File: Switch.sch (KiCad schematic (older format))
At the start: 4 parts, among them SW801 KH-PS1611-54

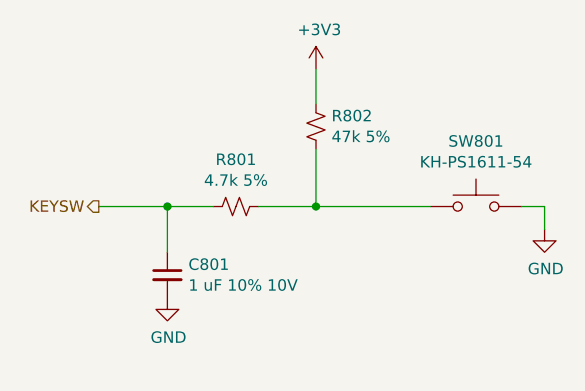
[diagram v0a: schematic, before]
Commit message: Added PCA9745B16B. Updated schematic. ERC Passes.
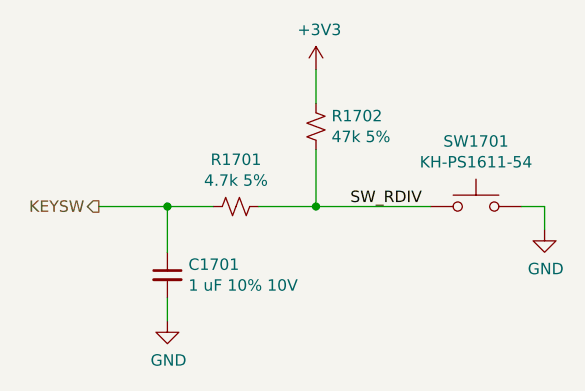
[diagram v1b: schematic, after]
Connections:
- net SW_RDIV: now reaches R801.1, R802.2, SW801.1
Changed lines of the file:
@@
 AR Path="/61A0B595/61A14F2D/61A0C35F" Ref="SW1601"  Part="1"
 AR Path="/61A0B595/61A14FBD/61A0C35F" Ref="SW1701"  Part="1"
-F 0 "SW801" H 5350 3285 50  0000 C CNN
+F 0 "SW1701" H 5350 3285 50  0000 C CNN
 F 1 "KH-PS1611-54" H 5350 3194 50  0000 C CNN
 F 2 "TMPPCB_R2:SW_MX" H 5350 3200 50  0001 C CNN
@@
 AR Path="/61A0B595/61A14F2D/61A0CD9F" Ref="#PWR01603"  Part="1"
 AR Path="/61A0B595/61A14FBD/61A0CD9F" Ref="#PWR01703"  Part="1"
-F 0 "#PWR0803" H 5650 2850 50  0001 C CNN
+F 0 "#PWR01703" H 5650 2850 50  0001 C CNN
 F 1 "GND" H 5655 2927 50  0000 C CNN
 F 2 "" H 5650 3100 50  0001 C CNN
@@
 	1    0    0    -1
 $EndComp
-Wire Wire Line
-	5550 3000 5650 3000
-Wire Wire Line
-	5650 3000 5650 3100
 $Comp
 L power:+3V3 #PWR0802
@@
 AR Path="/61A0B595/61A14F2D/61A0DCFF" Ref="#PWR01602"  Part="1"
 AR Path="/61A0B595/61A14FBD/61A0DCFF" Ref="#PWR01702"  Part="1"
-F 0 "#PWR0802" H 4650 2250 50  0001 C CNN
+F 0 "#PWR01702" H 4650 2250 50  0001 C CNN
 F 1 "+3V3" H 4665 2573 50  0000 C CNN
 F 2 "" H 4650 2400 50  0001 C CNN
@@
 AR Path="/61A0B595/61A14F2D/61A0F3A7" Ref="R1602"  Part="1"
 AR Path="/61A0B595/61A14FBD/61A0F3A7" Ref="R1702"  Part="1"
-F 0 "R802" H 4718 2696 50  0000 L CNN
+F 0 "R1702" H 4718 2696 50  0000 L CNN
 F 1 "47k 5%" H 4718 2605 50  0000 L CNN
 F 2 "Resistor_SMD:R_0805_2012Metric_Pad1.20x1.40mm_HandSolder" H 4650 2650 50  0001 C CNN
@@
 AR Path="/61A0B595/61A14F2D/61A1015C" Ref="C1601"  Part="1"
 AR Path="/61A0B595/61A14FBD/61A1015C" Ref="C1701"  Part="1"
-F 0 "C801" H 4092 3346 50  0000 L CNN
+F 0 "C1701" H 4092 3346 50  0000 L CNN
 F 1 "1 uF 10% 10V" H 4092 3255 50  0000 L CNN
 F 2 "Capacitor_SMD:C_0805_2012Metric_Pad1.18x1.45mm_HandSolder" H 4000 3300 50  0001 C CNN
@@
 L power:GND #PWR0801
 U 1 1 61A104A3
-P 4000 3400
+P 4000 3500
 AR Path="/61A0B595/61A0B6A8/61A104A3" Ref="#PWR0801"  Part="1"
 AR Path="/61A0B595/61A148A8/61A104A3" Ref="#PWR?"  Part="1"
@@
 AR Path="/61A0B595/61A14F2D/61A104A3" Ref="#PWR01601"  Part="1"
 AR Path="/61A0B595/61A14FBD/61A104A3" Ref="#PWR01701"  Part="1"
-F 0 "#PWR0801" H 4000 3150 50  0001 C CNN
-F 1 "GND" H 4005 3227 50  0000 C CNN
-F 2 "" H 4000 3400 50  0001 C CNN
-F 3 "" H 4000 3400 50  0001 C CNN
-	1    4000 3400
+F 0 "#PWR01701" H 4000 3250 50  0001 C CNN
+F 1 "GND" H 4005 3327 50  0000 C CNN
+F 2 "" H 4000 3500 50  0001 C CNN
+F 3 "" H 4000 3500 50  0001 C CNN
+	1    4000 3500
 	1    0    0    -1
 $EndComp
@@
 AR Path="/61A0B595/61A14F2D/61A0EB0D" Ref="R1601"  Part="1"
 AR Path="/61A0B595/61A14FBD/61A0EB0D" Ref="R1701"  Part="1"
-F 0 "R801" V 4095 3000 50  0000 C CNN
+F 0 "R1701" V 4095 3000 50  0000 C CNN
 F 1 "4.7k 5%" V 4186 3000 50  0000 C CNN
 F 2 "Resistor_SMD:R_0805_2012Metric_Pad1.20x1.40mm_HandSolder" H 4300 3000 50  0001 C CNN
@@
 	4000 3000 3700 3000
 Connection ~ 4000 3000
+Wire Wire Line
+	4000 3400 4000 3500
+Text Label 4800 3000 0    50   ~ 0
+SW_RDIV
+Wire Wire Line
+	5550 3000 5650 3000
+Wire Wire Line
+	5650 3000 5650 3100
 $EndSCHEMATC

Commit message: initial layout
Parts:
- renumbered C801 to C601, R801 to R601, R802 to R602, SW801 to SW601

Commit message: Starting routing
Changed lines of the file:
@@
 $Descr A4 11693 8268
 encoding utf-8
-Sheet 15 29
+Sheet 7 30
 Title ""
 Date ""
@@
 AR Path="/61A0B595/61A14F2D/61A0C35F" Ref="SW1401"  Part="1"
 AR Path="/61A0B595/61A14FBD/61A0C35F" Ref="SW1501"  Part="1"
-F 0 "SW1501" H 5350 3285 50  0000 C CNN
+F 0 "SW701" H 5350 3285 50  0000 C CNN
 F 1 "KH-PS1611-54" H 5350 3194 50  0000 C CNN
 F 2 "TMPPCB_R2:SW_MX" H 5350 3200 50  0001 C CNN
@@
 AR Path="/61A0B595/61A14F2D/61A0CD9F" Ref="#PWR01403"  Part="1"
 AR Path="/61A0B595/61A14FBD/61A0CD9F" Ref="#PWR01503"  Part="1"
-F 0 "#PWR01503" H 5650 2850 50  0001 C CNN
+F 0 "#PWR0703" H 5650 2850 50  0001 C CNN
 F 1 "GND" H 5655 2927 50  0000 C CNN
 F 2 "" H 5650 3100 50  0001 C CNN
@@
 AR Path="/61A0B595/61A14F2D/61A0DCFF" Ref="#PWR01402"  Part="1"
 AR Path="/61A0B595/61A14FBD/61A0DCFF" Ref="#PWR01502"  Part="1"
-F 0 "#PWR01502" H 4650 2250 50  0001 C CNN
+F 0 "#PWR0702" H 4650 2250 50  0001 C CNN
 F 1 "+3V3" H 4665 2573 50  0000 C CNN
 F 2 "" H 4650 2400 50  0001 C CNN
@@
 AR Path="/61A0B595/61A14F2D/61A0F3A7" Ref="R1402"  Part="1"
 AR Path="/61A0B595/61A14FBD/61A0F3A7" Ref="R1502"  Part="1"
-F 0 "R1502" H 4718 2696 50  0000 L CNN
+F 0 "R702" H 4718 2696 50  0000 L CNN
 F 1 "47k 5%" H 4718 2605 50  0000 L CNN
 F 2 "Resistor_SMD:R_0805_2012Metric_Pad1.20x1.40mm_HandSolder" H 4650 2650 50  0001 C CNN
@@
 AR Path="/61A0B595/61A14F2D/61A1015C" Ref="C1401"  Part="1"
 AR Path="/61A0B595/61A14FBD/61A1015C" Ref="C1501"  Part="1"
-F 0 "C1501" H 4092 3346 50  0000 L CNN
+F 0 "C701" H 4092 3346 50  0000 L CNN
 F 1 "1 uF 10% 10V" H 4092 3255 50  0000 L CNN
 F 2 "Capacitor_SMD:C_0805_2012Metric_Pad1.18x1.45mm_HandSolder" H 4000 3300 50  0001 C CNN
@@
 AR Path="/61A0B595/61A14F2D/61A104A3" Ref="#PWR01401"  Part="1"
 AR Path="/61A0B595/61A14FBD/61A104A3" Ref="#PWR01501"  Part="1"
-F 0 "#PWR01501" H 4000 3250 50  0001 C CNN
+F 0 "#PWR0701" H 4000 3250 50  0001 C CNN
 F 1 "GND" H 4005 3327 50  0000 C CNN
 F 2 "" H 4000 3500 50  0001 C CNN
@@
 AR Path="/61A0B595/61A14F2D/61A0EB0D" Ref="R1401"  Part="1"
 AR Path="/61A0B595/61A14FBD/61A0EB0D" Ref="R1501"  Part="1"
-F 0 "R1501" V 4095 3000 50  0000 C CNN
+F 0 "R701" V 4095 3000 50  0000 C CNN
 F 1 "4.7k 5%" V 4186 3000 50  0000 C CNN
 F 2 "Resistor_SMD:R_0805_2012Metric_Pad1.20x1.40mm_HandSolder" H 4300 3000 50  0001 C CNN

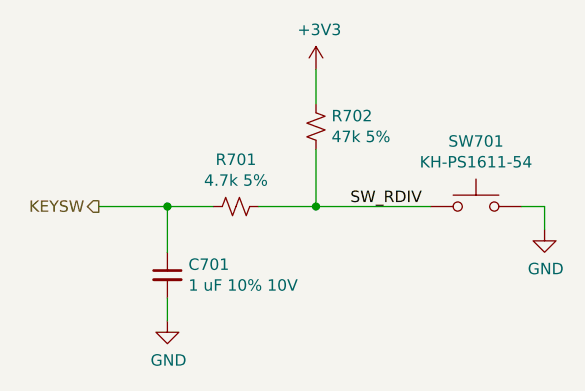
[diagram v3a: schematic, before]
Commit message: Layout completed. Design check passes.
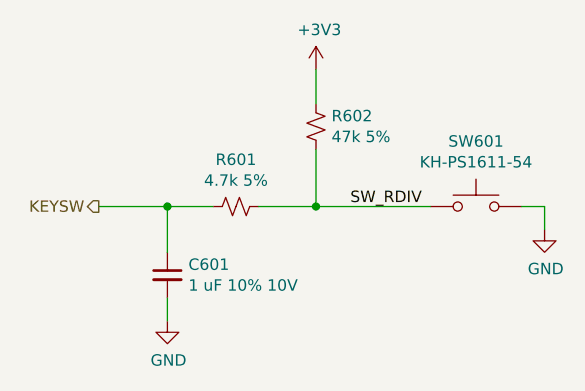
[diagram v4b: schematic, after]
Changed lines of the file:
@@
 $Descr A4 11693 8268
 encoding utf-8
-Sheet 7 30
+Sheet 5 30
 Title ""
 Date ""
@@
 AR Path="/61A0B595/61A14F2D/61A0C35F" Ref="SW1401"  Part="1"
 AR Path="/61A0B595/61A14FBD/61A0C35F" Ref="SW1501"  Part="1"
-F 0 "SW701" H 5350 3285 50  0000 C CNN
+F 0 "SW601" H 5350 3285 50  0000 C CNN
 F 1 "KH-PS1611-54" H 5350 3194 50  0000 C CNN
 F 2 "TMPPCB_R2:SW_MX" H 5350 3200 50  0001 C CNN
@@
 AR Path="/61A0B595/61A14F2D/61A0CD9F" Ref="#PWR01403"  Part="1"
 AR Path="/61A0B595/61A14FBD/61A0CD9F" Ref="#PWR01503"  Part="1"
-F 0 "#PWR0703" H 5650 2850 50  0001 C CNN
+F 0 "#PWR0603" H 5650 2850 50  0001 C CNN
 F 1 "GND" H 5655 2927 50  0000 C CNN
 F 2 "" H 5650 3100 50  0001 C CNN
@@
 AR Path="/61A0B595/61A14F2D/61A0DCFF" Ref="#PWR01402"  Part="1"
 AR Path="/61A0B595/61A14FBD/61A0DCFF" Ref="#PWR01502"  Part="1"
-F 0 "#PWR0702" H 4650 2250 50  0001 C CNN
+F 0 "#PWR0602" H 4650 2250 50  0001 C CNN
 F 1 "+3V3" H 4665 2573 50  0000 C CNN
 F 2 "" H 4650 2400 50  0001 C CNN
@@
 AR Path="/61A0B595/61A14F2D/61A0F3A7" Ref="R1402"  Part="1"
 AR Path="/61A0B595/61A14FBD/61A0F3A7" Ref="R1502"  Part="1"
-F 0 "R702" H 4718 2696 50  0000 L CNN
+F 0 "R602" H 4718 2696 50  0000 L CNN
 F 1 "47k 5%" H 4718 2605 50  0000 L CNN
 F 2 "Resistor_SMD:R_0805_2012Metric_Pad1.20x1.40mm_HandSolder" H 4650 2650 50  0001 C CNN
@@
 AR Path="/61A0B595/61A14F2D/61A1015C" Ref="C1401"  Part="1"
 AR Path="/61A0B595/61A14FBD/61A1015C" Ref="C1501"  Part="1"
-F 0 "C701" H 4092 3346 50  0000 L CNN
+F 0 "C601" H 4092 3346 50  0000 L CNN
 F 1 "1 uF 10% 10V" H 4092 3255 50  0000 L CNN
 F 2 "Capacitor_SMD:C_0805_2012Metric_Pad1.18x1.45mm_HandSolder" H 4000 3300 50  0001 C CNN
@@
 AR Path="/61A0B595/61A14F2D/61A104A3" Ref="#PWR01401"  Part="1"
 AR Path="/61A0B595/61A14FBD/61A104A3" Ref="#PWR01501"  Part="1"
-F 0 "#PWR0701" H 4000 3250 50  0001 C CNN
+F 0 "#PWR0601" H 4000 3250 50  0001 C CNN
 F 1 "GND" H 4005 3327 50  0000 C CNN
 F 2 "" H 4000 3500 50  0001 C CNN
@@
 AR Path="/61A0B595/61A14F2D/61A0EB0D" Ref="R1401"  Part="1"
 AR Path="/61A0B595/61A14FBD/61A0EB0D" Ref="R1501"  Part="1"
-F 0 "R701" V 4095 3000 50  0000 C CNN
+F 0 "R601" V 4095 3000 50  0000 C CNN
 F 1 "4.7k 5%" V 4186 3000 50  0000 C CNN
 F 2 "Resistor_SMD:R_0805_2012Metric_Pad1.20x1.40mm_HandSolder" H 4300 3000 50  0001 C CNN

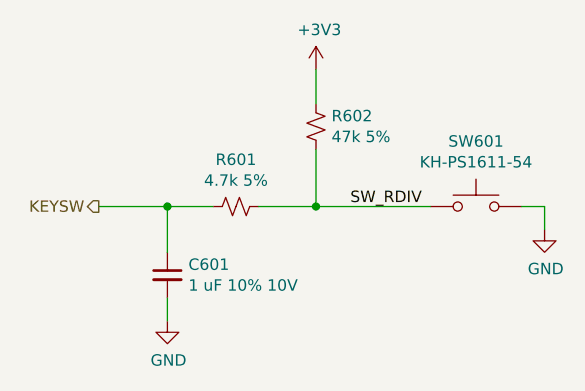
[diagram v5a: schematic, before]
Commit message: Re-arrange pins and cleanup routing
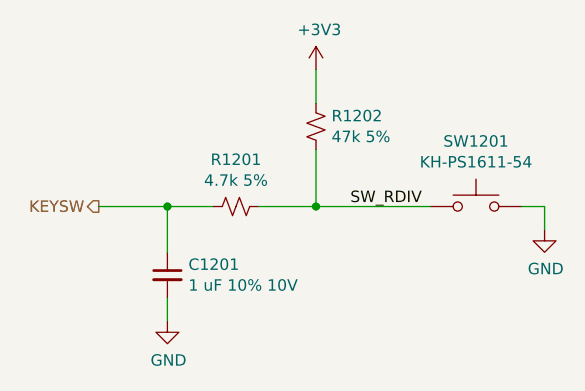
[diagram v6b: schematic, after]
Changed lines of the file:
@@
 $Descr A4 11693 8268
 encoding utf-8
-Sheet 5 30
+Sheet 11 30
 Title ""
 Date ""
@@
 AR Path="/61A0B595/61A14F2D/61A0C35F" Ref="SW1401"  Part="1"
 AR Path="/61A0B595/61A14FBD/61A0C35F" Ref="SW1501"  Part="1"
-F 0 "SW601" H 5350 3285 50  0000 C CNN
+F 0 "SW1201" H 5350 3285 50  0000 C CNN
 F 1 "KH-PS1611-54" H 5350 3194 50  0000 C CNN
 F 2 "TMPPCB_R2:SW_MX" H 5350 3200 50  0001 C CNN
@@
 AR Path="/61A0B595/61A14F2D/61A0CD9F" Ref="#PWR01403"  Part="1"
 AR Path="/61A0B595/61A14FBD/61A0CD9F" Ref="#PWR01503"  Part="1"
-F 0 "#PWR01503" H 5650 2850 50  0001 C CNN
+F 0 "#PWR01203" H 5650 2850 50  0001 C CNN
 F 1 "GND" H 5655 2927 50  0000 C CNN
 F 2 "" H 5650 3100 50  0001 C CNN
@@
 AR Path="/61A0B595/61A14F2D/61A0DCFF" Ref="#PWR01402"  Part="1"
 AR Path="/61A0B595/61A14FBD/61A0DCFF" Ref="#PWR01502"  Part="1"
-F 0 "#PWR01502" H 4650 2250 50  0001 C CNN
+F 0 "#PWR01202" H 4650 2250 50  0001 C CNN
 F 1 "+3V3" H 4665 2573 50  0000 C CNN
 F 2 "" H 4650 2400 50  0001 C CNN
@@
 AR Path="/61A0B595/61A14F2D/61A0F3A7" Ref="R1402"  Part="1"
 AR Path="/61A0B595/61A14FBD/61A0F3A7" Ref="R1502"  Part="1"
-F 0 "R602" H 4718 2696 50  0000 L CNN
+F 0 "R1202" H 4718 2696 50  0000 L CNN
 F 1 "47k 5%" H 4718 2605 50  0000 L CNN
 F 2 "Resistor_SMD:R_0805_2012Metric_Pad1.20x1.40mm_HandSolder" H 4650 2650 50  0001 C CNN
@@
 AR Path="/61A0B595/61A14F2D/61A1015C" Ref="C1401"  Part="1"
 AR Path="/61A0B595/61A14FBD/61A1015C" Ref="C1501"  Part="1"
-F 0 "C601" H 4092 3346 50  0000 L CNN
+F 0 "C1201" H 4092 3346 50  0000 L CNN
 F 1 "1 uF 10% 10V" H 4092 3255 50  0000 L CNN
 F 2 "Capacitor_SMD:C_0805_2012Metric_Pad1.18x1.45mm_HandSolder" H 4000 3300 50  0001 C CNN
@@
 AR Path="/61A0B595/61A14F2D/61A104A3" Ref="#PWR01401"  Part="1"
 AR Path="/61A0B595/61A14FBD/61A104A3" Ref="#PWR01501"  Part="1"
-F 0 "#PWR01501" H 4000 3250 50  0001 C CNN
+F 0 "#PWR01201" H 4000 3250 50  0001 C CNN
 F 1 "GND" H 4005 3327 50  0000 C CNN
 F 2 "" H 4000 3500 50  0001 C CNN
@@
 AR Path="/61A0B595/61A14F2D/61A0EB0D" Ref="R1401"  Part="1"
 AR Path="/61A0B595/61A14FBD/61A0EB0D" Ref="R1501"  Part="1"
-F 0 "R601" V 4095 3000 50  0000 C CNN
+F 0 "R1201" V 4095 3000 50  0000 C CNN
 F 1 "4.7k 5%" V 4186 3000 50  0000 C CNN
 F 2 "Resistor_SMD:R_0805_2012Metric_Pad1.20x1.40mm_HandSolder" H 4300 3000 50  0001 C CNN

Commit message: Fix design error in PI4ULS5V201TAEX. Reset and reassigned all annotations.
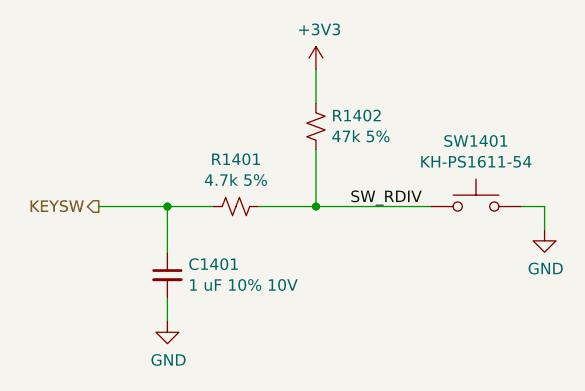
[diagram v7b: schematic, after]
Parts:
- renumbered C601 to C501, R601 to R501, R602 to R502, SW601 to SW501

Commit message: Remove resistor for SPI MOSI, MISO, and CS for LED Driver
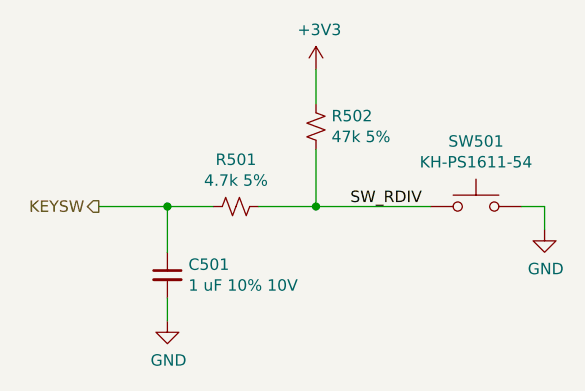
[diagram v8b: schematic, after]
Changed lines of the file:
@@
 $Descr A4 11693 8268
 encoding utf-8
-Sheet 11 30
+Sheet 5 30
 Title ""
 Date ""
@@
 AR Path="/61A0B595/61A14F2D/61A0C35F" Ref="SW1301"  Part="1"
 AR Path="/61A0B595/61A14FBD/61A0C35F" Ref="SW1401"  Part="1"
-F 0 "SW1401" H 5350 3285 50  0000 C CNN
+F 0 "SW501" H 5350 3285 50  0000 C CNN
 F 1 "KH-PS1611-54" H 5350 3194 50  0000 C CNN
 F 2 "TMPPCB_R2:SW_MX" H 5350 3200 50  0001 C CNN
@@
 AR Path="/61A0B595/61A14F2D/61A0CD9F" Ref="#PWR01303"  Part="1"
 AR Path="/61A0B595/61A14FBD/61A0CD9F" Ref="#PWR01403"  Part="1"
-F 0 "#PWR01403" H 5650 2850 50  0001 C CNN
+F 0 "#PWR0503" H 5650 2850 50  0001 C CNN
 F 1 "GND" H 5655 2927 50  0000 C CNN
 F 2 "" H 5650 3100 50  0001 C CNN
@@
 AR Path="/61A0B595/61A14F2D/61A0DCFF" Ref="#PWR01302"  Part="1"
 AR Path="/61A0B595/61A14FBD/61A0DCFF" Ref="#PWR01402"  Part="1"
-F 0 "#PWR01402" H 4650 2250 50  0001 C CNN
+F 0 "#PWR0502" H 4650 2250 50  0001 C CNN
 F 1 "+3V3" H 4665 2573 50  0000 C CNN
 F 2 "" H 4650 2400 50  0001 C CNN
@@
 AR Path="/61A0B595/61A14F2D/61A0F3A7" Ref="R1302"  Part="1"
 AR Path="/61A0B595/61A14FBD/61A0F3A7" Ref="R1402"  Part="1"
-F 0 "R1402" H 4718 2696 50  0000 L CNN
+F 0 "R502" H 4718 2696 50  0000 L CNN
 F 1 "47k 5%" H 4718 2605 50  0000 L CNN
 F 2 "Resistor_SMD:R_0805_2012Metric_Pad1.20x1.40mm_HandSolder" H 4650 2650 50  0001 C CNN
@@
 AR Path="/61A0B595/61A14F2D/61A1015C" Ref="C1301"  Part="1"
 AR Path="/61A0B595/61A14FBD/61A1015C" Ref="C1401"  Part="1"
-F 0 "C1401" H 4092 3346 50  0000 L CNN
+F 0 "C501" H 4092 3346 50  0000 L CNN
 F 1 "1 uF 10% 10V" H 4092 3255 50  0000 L CNN
 F 2 "Capacitor_SMD:C_0805_2012Metric_Pad1.18x1.45mm_HandSolder" H 4000 3300 50  0001 C CNN
@@
 AR Path="/61A0B595/61A14F2D/61A104A3" Ref="#PWR01301"  Part="1"
 AR Path="/61A0B595/61A14FBD/61A104A3" Ref="#PWR01401"  Part="1"
-F 0 "#PWR01401" H 4000 3250 50  0001 C CNN
+F 0 "#PWR0501" H 4000 3250 50  0001 C CNN
 F 1 "GND" H 4005 3327 50  0000 C CNN
 F 2 "" H 4000 3500 50  0001 C CNN
@@
 AR Path="/61A0B595/61A14F2D/61A0EB0D" Ref="R1301"  Part="1"
 AR Path="/61A0B595/61A14FBD/61A0EB0D" Ref="R1401"  Part="1"
-F 0 "R1401" V 4095 3000 50  0000 C CNN
+F 0 "R501" V 4095 3000 50  0000 C CNN
 F 1 "4.7k 5%" V 4186 3000 50  0000 C CNN
 F 2 "Resistor_SMD:R_0805_2012Metric_Pad1.20x1.40mm_HandSolder" H 4300 3000 50  0001 C CNN
